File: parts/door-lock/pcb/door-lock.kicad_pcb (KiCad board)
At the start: 2 copper layers, 63.2 x 40 mm, 13 parts, among them J2 RJ45_Shielded, U1 L293D

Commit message: door lock refinements.
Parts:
- mh1, mh2, mh3, mh4: value MountingHole_2.2mm_M2 -> MountingHole_3.2mm_M3; footprint MountingHole:MountingHole_2.2mm_M2 -> MountingHole:MountingHole_3.2mm_M3
- moved EXT_JACK1 9.56 mm to (117.9, 58.2)
- moved SHIELD1 3.61 mm to (76.6, 59.3)
- moved U1 3.07 mm to (73.0, 52.7)
- moved C1 1.94 mm to (73.4, 27.0)
- moved ziptie_hole1 1.88 mm to (125.1, 39.3)
- moved ziptie_hole2 1.88 mm to (125.1, 52.0)
- moved mh3 1.33 mm to (125.0, 26.4)
- moved mh1 1.30 mm to (66.9, 26.4)
- moved mh4 1.25 mm to (125.0, 59.4)
- moved mh2 1.13 mm to (66.9, 59.4)
- moved HALL_MODULE_PT1 0.76 mm to (80.3, 26.5)
- moved HALL_MODULE_PT2 0.76 mm to (107.0, 32.8)
- moved J2 0.69 mm to (79.8, 50.1)
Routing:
- net /GND: track 96.0 -> 0.00 mm, vias 1 -> 0
- net /5V: track 91.8 -> 0.00 mm
- net /SENSE: track 36.1 -> 0.00 mm
- net unconnected-(J2-PadSH): track 33.8 -> 0.00 mm
- net /OUT: track 33.8 -> 0.00 mm
- net Net-(EXT_JACK1-MOTOR+): track 33.7 -> 0.00 mm, vias 1 -> 0
- net Net-(EXT_JACK1-MOTOR-): track 32.7 -> 0.00 mm, vias 1 -> 0
- net /12V: track 19.8 -> 0.00 mm
- net /UNLOCK: track 17.1 -> 0.00 mm
- net /LOCK: track 5.20 -> 0.00 mm
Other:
- board size 63.2 x 40 mm -> 65 x 40 mm
- board text added: "Door Lock Driver rev 1.91"
- board text added: "R B G"
- board text added: "pending: change out RJ45 footprint when verified"
- board text removed: "Door Lock Driver rev 1.8"
- board text removed: "H1R H2B H3G M+ M-"

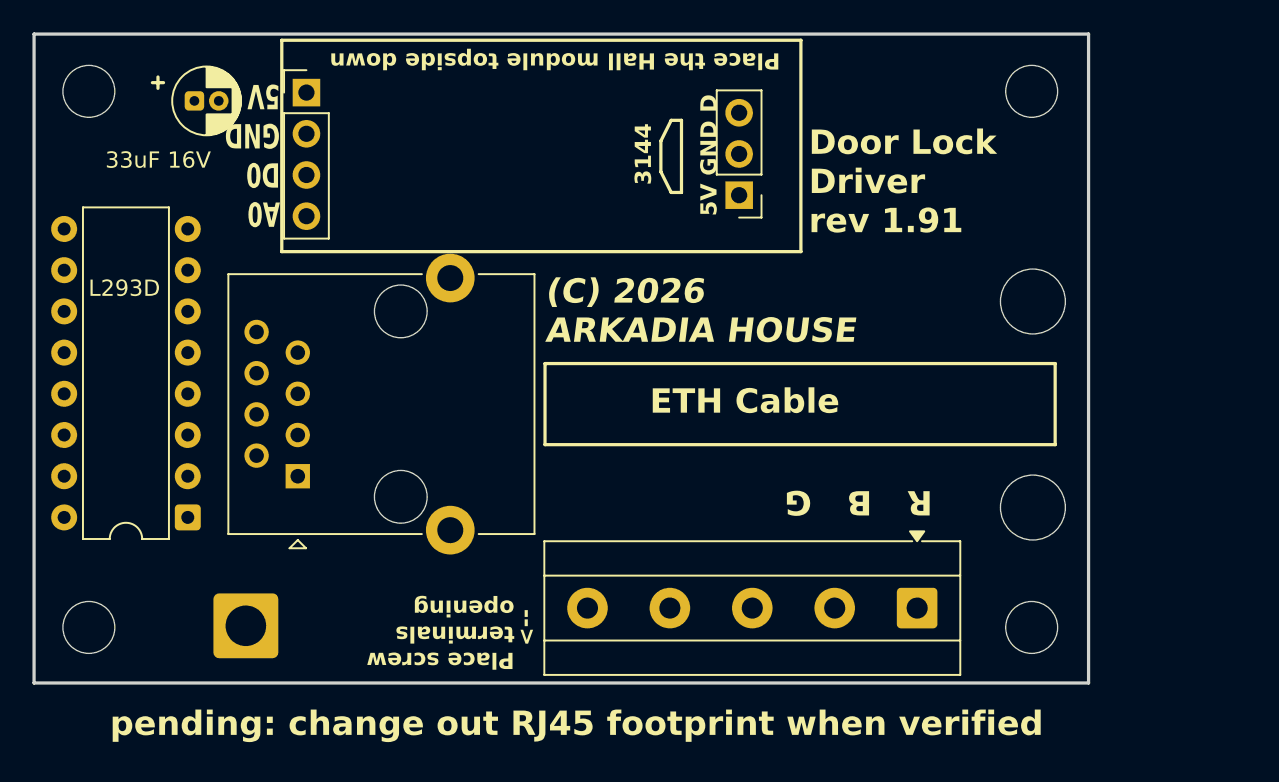
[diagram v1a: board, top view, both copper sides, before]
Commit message: pcb revisions to update to better RJ45 jack, update QR code.
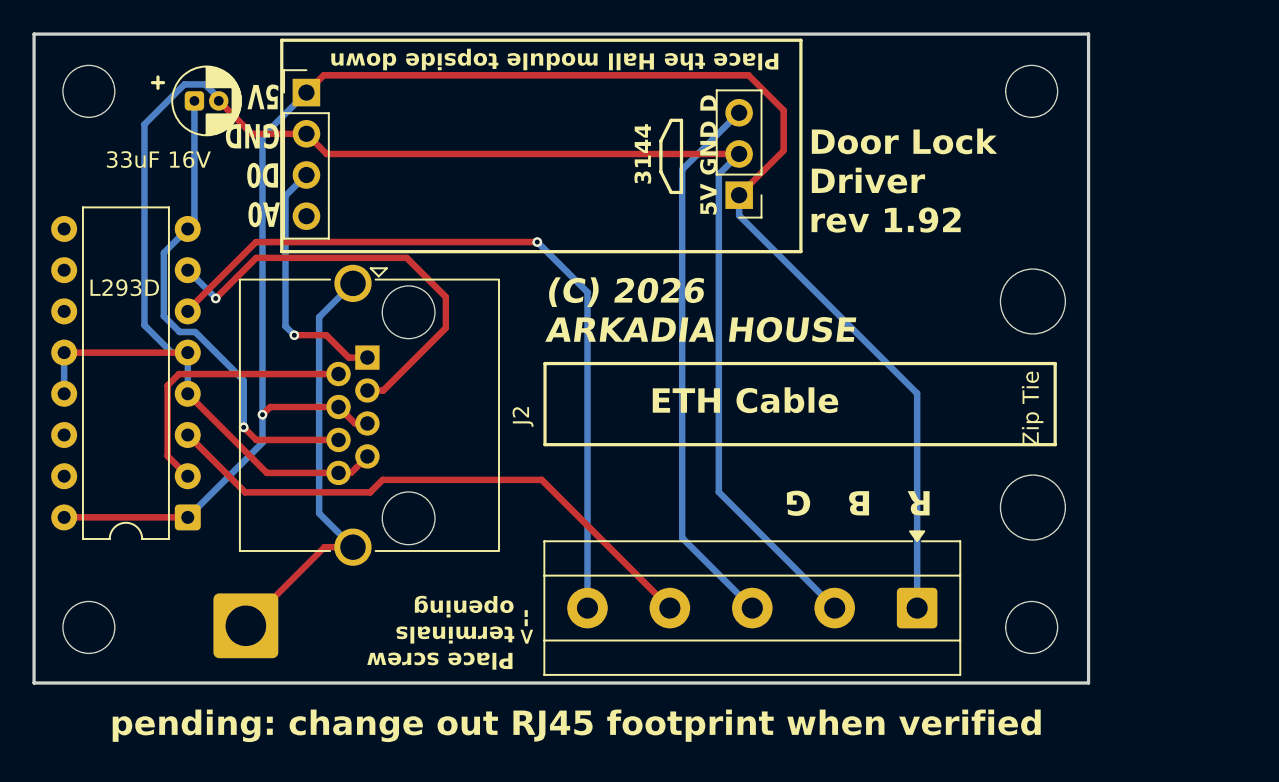
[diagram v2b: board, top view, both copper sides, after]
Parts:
- J2: footprint Connector_RJ:RJ45_Ninigi_GE -> Connector_RJ:RJ45_Amphenol_RJHSE5380
- moved J2 8.48 mm to (84.0, 42.8), turned to -90 degrees
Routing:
- net /GND: track 0.00 -> 112.7 mm
- net /5V: track 0.00 -> 111.0 mm, vias 0 -> 1
- net Net-(EXT_JACK1-MOTOR-): track 0.00 -> 47.1 mm, vias 0 -> 1
- net Net-(EXT_JACK1-MOTOR+): track 0.00 -> 34.8 mm
- net /OUT: track 0.00 -> 33.8 mm
- net /12V: track 0.00 -> 29.1 mm, vias 0 -> 1
- net /UNLOCK: track 0.00 -> 27.0 mm, vias 0 -> 1
- net unconnected-(J2-PadSH): track 0.00 -> 26.6 mm
- net /LOCK: track 0.00 -> 16.9 mm
- net /SENSE: track 0.00 -> 15.7 mm, vias 0 -> 1
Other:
- board text added: "Door Lock Driver rev 1.92"
- board text added: "Zip Tie"
- board text removed: "Door Lock Driver rev 1.91"
